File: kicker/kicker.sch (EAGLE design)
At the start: 25 parts, among them T1 NPN_BC817,215, T2 NPN_BC817,215, T3 NPN_BC817,215, T4 NPN_BC817,215, X1 JST-XH-06-PIN-LONG-PAD

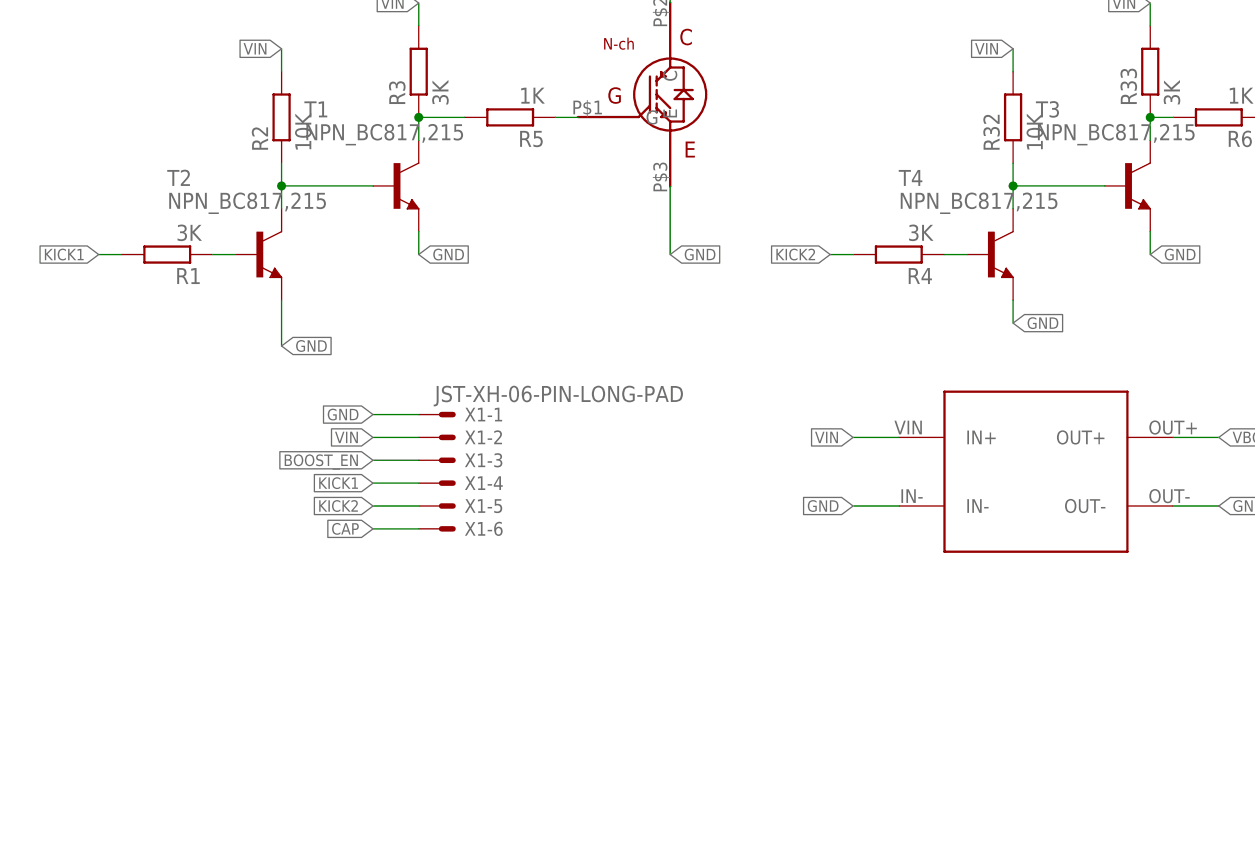
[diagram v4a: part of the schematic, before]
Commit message: Adding optocoupler on the kick line
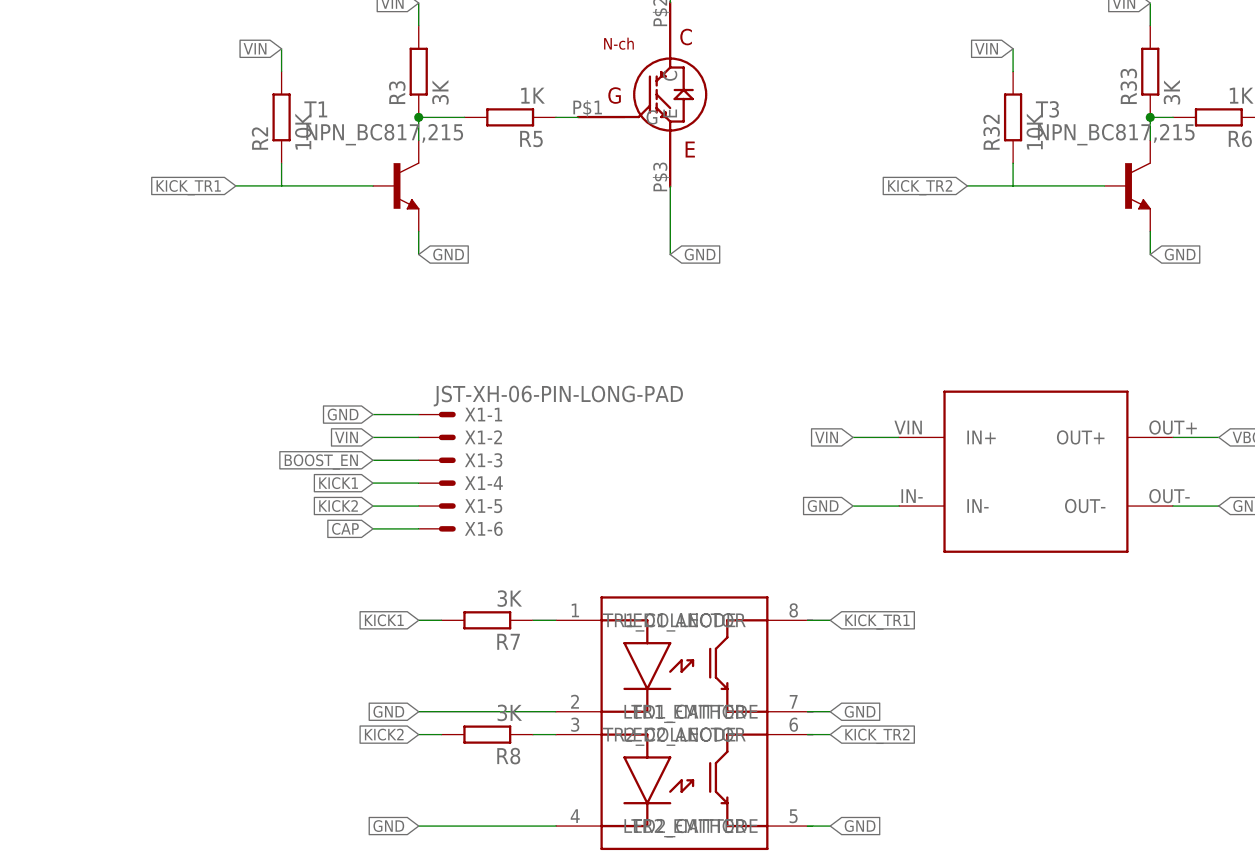
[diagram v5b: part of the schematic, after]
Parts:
- removed R1, R4: 3K, rhoban:RESISTANCE-R0805
- removed T2, T4: NPN_BC817,215, rhoban:NPN_BC817,215
- added R7, R8: 3K, rhoban:RESISTANCE-R0805
- added U$4: ACPL-227-500E, rhoban:ACPL-227-500E
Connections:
- removed net N$1: R2.1, T1.B, T2.C
- removed net N$3: R32.1, T3.B, T4.C
- removed net N$5: R1.1, T2.B
- removed net N$6: R4.1, T4.B
- new net KICK_TR1: R2.1, T1.B
- new net KICK_TR2: R32.1, T3.B
- new net N$10: R8.1, U$4.LED2_ANODE
- new net N$9: R7.1, U$4.LED1_ANODE
- net GND: now also U$4.LED1_CATHODE, U$4.LED2_CATHODE; no longer T2.E, T4.E
- net KICK1: now also R7.2; no longer R1.2
- net KICK2: now also R8.2; no longer R4.2
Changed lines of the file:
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@@
-<attribute name="FARNELL" value="2446965"/>
-</part>
-<part name="T2" library="rhoban" deviceset="NPN" device="_BC817,215">
-<attribute name="FARNELL" value="1081223"/>
-</part>
-<part name="R1" library="rhoban" deviceset="RESISTANCE" device="-R0805" value="3K">
-<attribute name="FARNELL" value="2446965"/>
-</part>
-<part name="T4" library="rhoban" deviceset="NPN" device="_BC817,215">
-<attribute name="FARNELL" value="1081223"/>
-</part>
-<part name="R4" library="rhoban" deviceset="RESISTANCE" device="-R0805" value="3K">
 <attribute name="FARNELL" value="2446965"/>
 </part>
@@
 </part>
 <part name="R6" library="rhoban" deviceset="RESISTANCE" device="-R0805" value="1K">
+<attribute name="FARNELL" value="2446965"/>
+</part>
+<part name="U$4" library="rhoban" deviceset="ACPL-227-500E" device="">
+<attribute name="FARNELL" value="1634749RL"/>
+</part>
+<part name="R7" library="rhoban" deviceset="RESISTANCE" device="-R0805" value="3K">
+<attribute name="FARNELL" value="2446965"/>
+</part>
+<part name="R8" library="rhoban" deviceset="RESISTANCE" device="-R0805" value="3K">
 <attribute name="FARNELL" value="2446965"/>
 </part>
@@
 <plain>
 <text x="-12.7" y="91.44" size="6.4516" layer="95">KICKER</text>
-<frame x1="-88.9" y1="-48.26" x2="99.06" y2="111.76" columns="8" rows="5" layer="94"/>
+<frame x1="-88.9" y1="-68.58" x2="96.52" y2="106.68" columns="8" rows="5" layer="94"/>
 </plain>
 <instances>
@@
 <attribute name="FARNELL" x="-50.8" y="20.32" size="1.778" layer="96" rot="R90" display="off"/>
 </instance>
-<instance part="T2" gate="G$1" x="-53.34" y="5.08">
-<attribute name="FARNELL" x="-55.88" y="7.62" size="1.778" layer="96" display="off"/>
-</instance>
-<instance part="R1" gate="G$1" x="-63.5" y="5.08" rot="R180">
-<attribute name="FARNELL" x="-63.5" y="7.62" size="1.778" layer="96" rot="R180" display="off"/>
-</instance>
-<instance part="T4" gate="G$1" x="27.94" y="5.08">
-<attribute name="FARNELL" x="25.4" y="7.62" size="1.778" layer="96" display="off"/>
-</instance>
-<instance part="R4" gate="G$1" x="17.78" y="5.08" rot="R180">
-<attribute name="FARNELL" x="17.78" y="5.08" size="1.778" layer="96" rot="R180" display="off"/>
-</instance>
 <instance part="R5" gate="G$1" x="-25.4" y="20.32" rot="R180">
 <attribute name="FARNELL" x="-27.94" y="20.32" size="1.778" layer="96" rot="R180" display="off"/>
@@
 <instance part="R6" gate="G$1" x="53.34" y="20.32" rot="R180">
 <attribute name="FARNELL" x="50.8" y="22.86" size="1.778" layer="96" rot="R180" display="off"/>
+</instance>
+<instance part="U$4" gate="G$1" x="-15.24" y="-60.96">
+<attribute name="FARNELL" x="-15.24" y="-60.96" size="1.27" layer="96" display="off"/>
+</instance>
+<instance part="R7" gate="G$1" x="-27.94" y="-35.56" rot="R180">
+<attribute name="FARNELL" x="-30.48" y="-33.02" size="1.778" layer="96" rot="R180" display="off"/>
+</instance>
+<instance part="R8" gate="G$1" x="-27.94" y="-48.26" rot="R180">
+<attribute name="FARNELL" x="-30.48" y="-45.72" size="1.778" layer="96" rot="R180" display="off"/>
 </instance>
 </instances>
@@
 </segment>
 <segment>
-<wire x1="12.7" y1="5.08" x2="10.16" y2="5.08" width="0.1524" layer="91"/>
-<label x="10.16" y="5.08" size="1.27" layer="95" rot="R180" xref="yes"/>
-<pinref part="R4" gate="G$1" pin="2"/>
+<pinref part="R8" gate="G$1" pin="2"/>
+<wire x1="-33.02" y1="-48.26" x2="-35.56" y2="-48.26" width="0.1524" layer="91"/>
+<label x="-35.56" y="-48.26" size="1.27" layer="95" rot="R180" xref="yes"/>
 </segment>
 </net>
@@
 </segment>
 <segment>
-<pinref part="T2" gate="G$1" pin="E"/>
-<wire x1="-50.8" y1="0" x2="-50.8" y2="-5.08" width="0.1524" layer="91"/>
-<label x="-50.8" y="-5.08" size="1.27" layer="95" xref="yes"/>
-</segment>
-<segment>
-<pinref part="T4" gate="G$1" pin="E"/>
-<wire x1="30.48" y1="0" x2="30.48" y2="-2.54" width="0.1524" layer="91"/>
-<label x="30.48" y="-2.54" size="1.27" layer="95" xref="yes"/>
+<pinref part="U$4" gate="G$1" pin="LED1_CATHODE"/>
+<wire x1="-20.32" y1="-45.72" x2="-35.56" y2="-45.72" width="0.1524" layer="91"/>
+<label x="-35.56" y="-45.72" size="1.27" layer="95" rot="R180" xref="yes"/>
+</segment>
+<segment>
+<pinref part="U$4" gate="G$1" pin="LED2_CATHODE"/>
+<wire x1="-20.32" y1="-58.42" x2="-35.56" y2="-58.42" width="0.1524" layer="91"/>
+<label x="-35.56" y="-58.42" size="1.27" layer="95" rot="R180" xref="yes"/>
+</segment>
+<segment>
+<wire x1="7.62" y1="-45.72" x2="10.16" y2="-45.72" width="0.1524" layer="91"/>
+<label x="10.16" y="-45.72" size="1.27" layer="95" xref="yes"/>
+</segment>
+<segment>
+<wire x1="7.62" y1="-58.42" x2="10.16" y2="-58.42" width="0.1524" layer="91"/>
+<label x="10.16" y="-58.42" size="1.27" layer="95" xref="yes"/>
 </segment>
 </net>
@@
 <net name="KICK1" class="0">
 <segment>
-<wire x1="-68.58" y1="5.08" x2="-71.12" y2="5.08" width="0.1524" layer="91"/>
-<label x="-71.12" y="5.08" size="1.27" layer="95" rot="R180" xref="yes"/>
-<pinref part="R1" gate="G$1" pin="2"/>
-</segment>
-<segment>
 <pinref part="X1" gate="-4" pin="S"/>
 <wire x1="-35.56" y1="-20.32" x2="-40.64" y2="-20.32" width="0.1524" layer="91"/>
 <label x="-40.64" y="-20.32" size="1.27" layer="95" rot="R180" xref="yes"/>
+</segment>
+<segment>
+<pinref part="R7" gate="G$1" pin="2"/>
+<wire x1="-33.02" y1="-35.56" x2="-35.56" y2="-35.56" width="0.1524" layer="91"/>
+<label x="-35.56" y="-35.56" size="1.27" layer="95" rot="R180" xref="yes"/>
 </segment>
 </net>
@@
 </segment>
 </net>
-<net name="N$1" class="0">
+<net name="N$7" class="0">
+<segment>
+<pinref part="U$1" gate="G$1" pin="G"/>
+<pinref part="R5" gate="G$1" pin="1"/>
+<wire x1="-17.78" y1="20.32" x2="-20.32" y2="20.32" width="0.1524" layer="91"/>
+</segment>
+</net>
+<net name="N$8" class="0">
+<segment>
+<pinref part="R6" gate="G$1" pin="1"/>
+<pinref part="U$11" gate="G$1" pin="G"/>
+<wire x1="58.42" y1="20.32" x2="63.5" y2="20.32" width="0.1524" layer="91"/>
+</segment>
+</net>
+<net name="N$9" class="0">
+<segment>
+<pinref part="U$4" gate="G$1" pin="LED1_ANODE"/>
+<pinref part="R7" gate="G$1" pin="1"/>
+<wire x1="-22.86" y1="-35.56" x2="-20.32" y2="-35.56" width="0.1524" layer="91"/>
+</segment>
+</net>
+<net name="N$10" class="0">
+<segment>
+<pinref part="U$4" gate="G$1" pin="LED2_ANODE"/>
+<pinref part="R8" gate="G$1" pin="1"/>
+<wire x1="-22.86" y1="-48.26" x2="-20.32" y2="-48.26" width="0.1524" layer="91"/>
+</segment>
+</net>
+<net name="KICK_TR1" class="0">
+<segment>
+<wire x1="7.62" y1="-35.56" x2="10.16" y2="-35.56" width="0.1524" layer="91"/>
+<label x="10.16" y="-35.56" size="1.27" layer="95" xref="yes"/>
+</segment>
 <segment>
 <pinref part="R2" gate="G$1" pin="1"/>
-<pinref part="T2" gate="G$1" pin="C"/>
-<wire x1="-50.8" y1="10.16" x2="-50.8" y2="12.7" width="0.1524" layer="91"/>
 <pinref part="T1" gate="G$1" pin="B"/>
 <wire x1="-50.8" y1="12.7" x2="-50.8" y2="15.24" width="0.1524" layer="91"/>
 <wire x1="-40.64" y1="12.7" x2="-50.8" y2="12.7" width="0.1524" layer="91"/>
-<junction x="-50.8" y="12.7"/>
-</segment>
-</net>
-<net name="N$5" class="0">
-<segment>
-<pinref part="T2" gate="G$1" pin="B"/>
-<pinref part="R1" gate="G$1" pin="1"/>
-<wire x1="-58.42" y1="5.08" x2="-55.88" y2="5.08" width="0.1524" layer="91"/>
-</segment>
-</net>
-<net name="N$6" class="0">
-<segment>
-<pinref part="T4" gate="G$1" pin="B"/>
-<wire x1="25.4" y1="5.08" x2="22.86" y2="5.08" width="0.1524" layer="91"/>
-<pinref part="R4" gate="G$1" pin="1"/>
-</segment>
-</net>
-<net name="N$3" class="0">
-<segment>
-<pinref part="T4" gate="G$1" pin="C"/>
+<wire x1="-50.8" y1="12.7" x2="-55.88" y2="12.7" width="0.1524" layer="91"/>
+<label x="-55.88" y="12.7" size="1.27" layer="95" rot="R180" xref="yes"/>
+</segment>
+</net>
+<net name="KICK_TR2" class="0">
+<segment>
+<wire x1="7.62" y1="-48.26" x2="10.16" y2="-48.26" width="0.1524" layer="91"/>
+<label x="10.16" y="-48.26" size="1.27" layer="95" xref="yes"/>
+</segment>
+<segment>
 <pinref part="R32" gate="G$1" pin="1"/>
-<wire x1="30.48" y1="10.16" x2="30.48" y2="12.7" width="0.1524" layer="91"/>
 <pinref part="T3" gate="G$1" pin="B"/>
 <wire x1="30.48" y1="12.7" x2="30.48" y2="15.24" width="0.1524" layer="91"/>
 <wire x1="40.64" y1="12.7" x2="30.48" y2="12.7" width="0.1524" layer="91"/>
-<junction x="30.48" y="12.7"/>
-</segment>
-</net>
-<net name="N$7" class="0">
-<segment>
-<pinref part="U$1" gate="G$1" pin="G"/>
-<pinref part="R5" gate="G$1" pin="1"/>
-<wire x1="-17.78" y1="20.32" x2="-20.32" y2="20.32" width="0.1524" layer="91"/>
-</segment>
-</net>
-<net name="N$8" class="0">
-<segment>
-<pinref part="R6" gate="G$1" pin="1"/>
-<pinref part="U$11" gate="G$1" pin="G"/>
-<wire x1="58.42" y1="20.32" x2="63.5" y2="20.32" width="0.1524" layer="91"/>
-</segment>
-</net>
+<wire x1="30.48" y1="12.7" x2="25.4" y2="12.7" width="0.1524" layer="91"/>
+<label x="25.4" y="12.7" size="1.27" layer="95" rot="R180" xref="yes"/>
+</segment>
+</net>

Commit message: Fix optocoupler
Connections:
- net GND: now also U$4.TR1_EMITTER, U$4.TR2_EMITTER
- net KICK_TR1: now also U$4.TR1_COLLECTOR
- net KICK_TR2: now also U$4.TR2_COLLECTOR
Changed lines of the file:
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@@
 </segment>
 <segment>
-<wire x1="7.62" y1="-45.72" x2="10.16" y2="-45.72" width="0.1524" layer="91"/>
+<wire x1="7.62" y1="-45.72" x2="8.255" y2="-45.72" width="0.1524" layer="91"/>
 <label x="10.16" y="-45.72" size="1.27" layer="95" xref="yes"/>
-</segment>
-<segment>
-<wire x1="7.62" y1="-58.42" x2="10.16" y2="-58.42" width="0.1524" layer="91"/>
+<pinref part="U$4" gate="G$1" pin="TR1_EMITTER"/>
+<wire x1="8.255" y1="-45.72" x2="10.16" y2="-45.72" width="0.1524" layer="91"/>
+<junction x="8.255" y="-45.72"/>
+</segment>
+<segment>
+<wire x1="7.62" y1="-58.42" x2="8.255" y2="-58.42" width="0.1524" layer="91"/>
 <label x="10.16" y="-58.42" size="1.27" layer="95" xref="yes"/>
+<pinref part="U$4" gate="G$1" pin="TR2_EMITTER"/>
+<wire x1="8.255" y1="-58.42" x2="10.16" y2="-58.42" width="0.1524" layer="91"/>
+<junction x="8.255" y="-58.42"/>
 </segment>
 </net>
@@
 <pinref part="U$4" gate="G$1" pin="LED1_ANODE"/>
 <pinref part="R7" gate="G$1" pin="1"/>
-<wire x1="-22.86" y1="-35.56" x2="-20.32" y2="-35.56" width="0.1524" layer="91"/>
+<wire x1="-20.32" y1="-35.56" x2="-22.86" y2="-35.56" width="0.1524" layer="91"/>
 </segment>
 </net>
@@
 <pinref part="U$4" gate="G$1" pin="LED2_ANODE"/>
 <pinref part="R8" gate="G$1" pin="1"/>
-<wire x1="-22.86" y1="-48.26" x2="-20.32" y2="-48.26" width="0.1524" layer="91"/>
+<wire x1="-20.32" y1="-48.26" x2="-22.86" y2="-48.26" width="0.1524" layer="91"/>
 </segment>
 </net>
 <net name="KICK_TR1" class="0">
 <segment>
-<wire x1="7.62" y1="-35.56" x2="10.16" y2="-35.56" width="0.1524" layer="91"/>
+<wire x1="7.62" y1="-35.56" x2="8.255" y2="-35.56" width="0.1524" layer="91"/>
 <label x="10.16" y="-35.56" size="1.27" layer="95" xref="yes"/>
+<pinref part="U$4" gate="G$1" pin="TR1_COLLECTOR"/>
+<wire x1="8.255" y1="-35.56" x2="10.16" y2="-35.56" width="0.1524" layer="91"/>
+<junction x="8.255" y="-35.56"/>
 </segment>
 <segment>
@@
 <net name="KICK_TR2" class="0">
 <segment>
-<wire x1="7.62" y1="-48.26" x2="10.16" y2="-48.26" width="0.1524" layer="91"/>
+<wire x1="7.62" y1="-48.26" x2="8.255" y2="-48.26" width="0.1524" layer="91"/>
 <label x="10.16" y="-48.26" size="1.27" layer="95" xref="yes"/>
-</segment>
-<segment>
+<pinref part="U$4" gate="G$1" pin="TR2_COLLECTOR"/>
+<wire x1="8.255" y1="-48.26" x2="10.16" y2="-48.26" width="0.1524" layer="91"/>
+<junction x="8.255" y="-48.26"/>
+</segment>
+<segment>

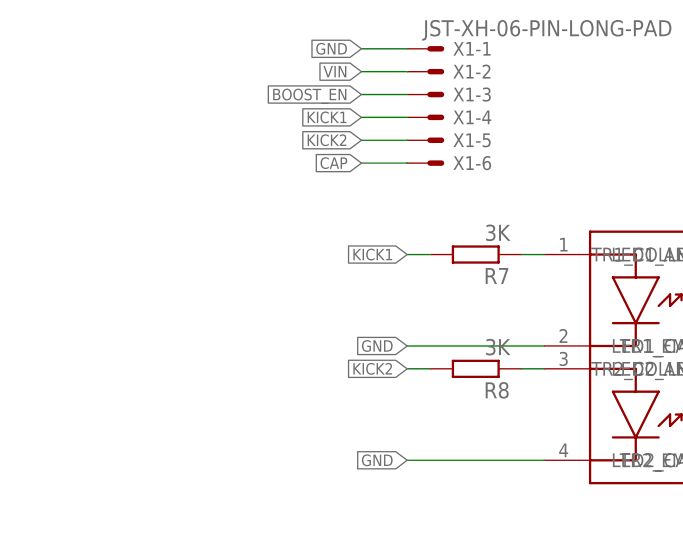
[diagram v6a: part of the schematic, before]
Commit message: Adding optional npn for kicking
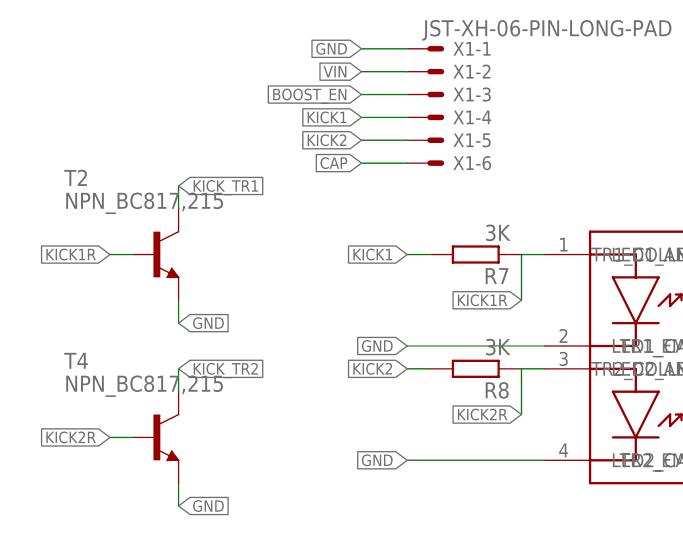
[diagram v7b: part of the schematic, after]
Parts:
- added T2, T4: NPN_BC817,215, rhoban:NPN_BC817,215
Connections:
- removed net N$10: R8.1, U$4.LED2_ANODE
- removed net N$9: R7.1, U$4.LED1_ANODE
- new net KICK1R: R7.1, T2.B, U$4.LED1_ANODE
- new net KICK2R: R8.1, T4.B, U$4.LED2_ANODE
- net GND: now also T2.E, T4.E
- net KICK_TR1: now also T2.C
- net KICK_TR2: now also T4.C
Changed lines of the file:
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@@
 <attribute name="FARNELL" value="2446965"/>
+</part>
+<part name="T2" library="rhoban" deviceset="NPN" device="_BC817,215">
+<attribute name="FARNELL" value="1081223"/>
+</part>
+<part name="T4" library="rhoban" deviceset="NPN" device="_BC817,215">
+<attribute name="FARNELL" value="1081223"/>
 </part>
 </parts>
@@
 <attribute name="FARNELL" x="-30.48" y="-45.72" size="1.778" layer="96" rot="R180" display="off"/>
 </instance>
+<instance part="T2" gate="G$1" x="-63.5" y="-35.56">
+<attribute name="FARNELL" x="-63.5" y="-35.56" size="1.778" layer="96" display="off"/>
+</instance>
+<instance part="T4" gate="G$1" x="-63.5" y="-55.88">
+<attribute name="FARNELL" x="-63.5" y="-55.88" size="1.778" layer="96" display="off"/>
+</instance>
 </instances>
 <busses>
@@
 <wire x1="8.255" y1="-58.42" x2="10.16" y2="-58.42" width="0.1524" layer="91"/>
 <junction x="8.255" y="-58.42"/>
+</segment>
+<segment>
+<pinref part="T2" gate="G$1" pin="E"/>
+<wire x1="-60.96" y1="-40.64" x2="-60.96" y2="-43.18" width="0.1524" layer="91"/>
+<label x="-60.96" y="-43.18" size="1.27" layer="95" xref="yes"/>
+</segment>
+<segment>
+<pinref part="T4" gate="G$1" pin="E"/>
+<wire x1="-60.96" y1="-60.96" x2="-60.96" y2="-63.5" width="0.1524" layer="91"/>
+<label x="-60.96" y="-63.5" size="1.27" layer="95" xref="yes"/>
 </segment>
 </net>
@@
 </segment>
 </net>
-<net name="N$9" class="0">
+<net name="KICK1R" class="0">
 <segment>
 <pinref part="U$4" gate="G$1" pin="LED1_ANODE"/>
 <pinref part="R7" gate="G$1" pin="1"/>
 <wire x1="-20.32" y1="-35.56" x2="-22.86" y2="-35.56" width="0.1524" layer="91"/>
-</segment>
-</net>
-<net name="N$10" class="0">
+<wire x1="-22.86" y1="-35.56" x2="-22.86" y2="-40.64" width="0.1524" layer="91"/>
+<label x="-22.86" y="-40.64" size="1.27" layer="95" rot="R180" xref="yes"/>
+</segment>
+<segment>
+<pinref part="T2" gate="G$1" pin="B"/>
+<wire x1="-66.04" y1="-35.56" x2="-68.58" y2="-35.56" width="0.1524" layer="91"/>
+<label x="-68.58" y="-35.56" size="1.27" layer="95" rot="R180" xref="yes"/>
+</segment>
+</net>
+<net name="KICK2R" class="0">
 <segment>
 <pinref part="U$4" gate="G$1" pin="LED2_ANODE"/>
 <pinref part="R8" gate="G$1" pin="1"/>
 <wire x1="-20.32" y1="-48.26" x2="-22.86" y2="-48.26" width="0.1524" layer="91"/>
+<wire x1="-22.86" y1="-48.26" x2="-22.86" y2="-53.34" width="0.1524" layer="91"/>
+<label x="-22.86" y="-53.34" size="1.27" layer="95" rot="R180" xref="yes"/>
+</segment>
+<segment>
+<pinref part="T4" gate="G$1" pin="B"/>
+<wire x1="-66.04" y1="-55.88" x2="-68.58" y2="-55.88" width="0.1524" layer="91"/>
+<label x="-68.58" y="-55.88" size="1.27" layer="95" rot="R180" xref="yes"/>
 </segment>
 </net>
@@
 <label x="-55.88" y="12.7" size="1.27" layer="95" rot="R180" xref="yes"/>
 </segment>
+<segment>
+<pinref part="T2" gate="G$1" pin="C"/>
+<wire x1="-60.96" y1="-30.48" x2="-60.96" y2="-27.94" width="0.1524" layer="91"/>
+<label x="-60.96" y="-27.94" size="1.27" layer="95" xref="yes"/>
+</segment>
 </net>
 <net name="KICK_TR2" class="0">
@@
 <label x="25.4" y="12.7" size="1.27" layer="95" rot="R180" xref="yes"/>
 </segment>
-</net>
+<segment>
+<pinref part="T4" gate="G$1" pin="C"/>
+<wire x1="-60.96" y1="-50.8" x2="-60.96" y2="-48.26" width="0.1524" layer="91"/>
+<label x="-60.96" y="-48.26" size="1.27" layer="95" xref="yes"/>
+</segment>
+</net>
